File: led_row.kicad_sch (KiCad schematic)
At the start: 8 parts

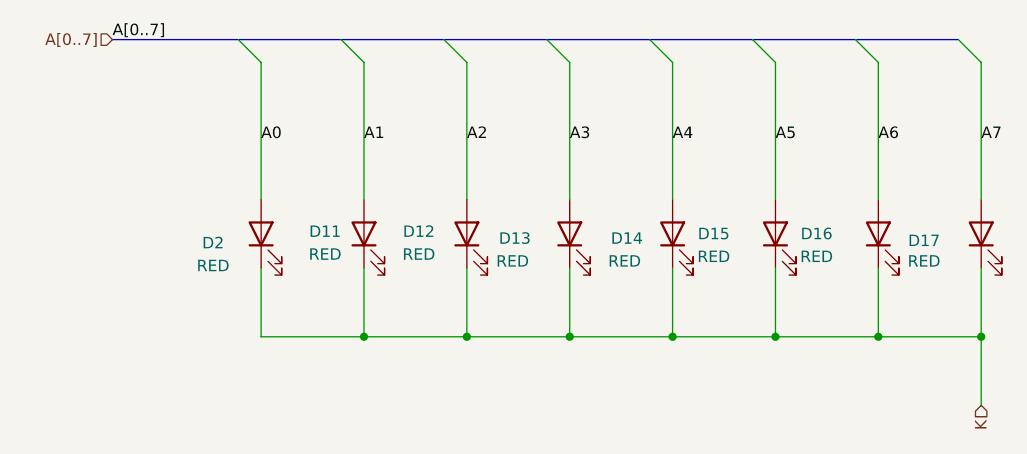
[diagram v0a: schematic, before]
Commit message: LED updates with some layout
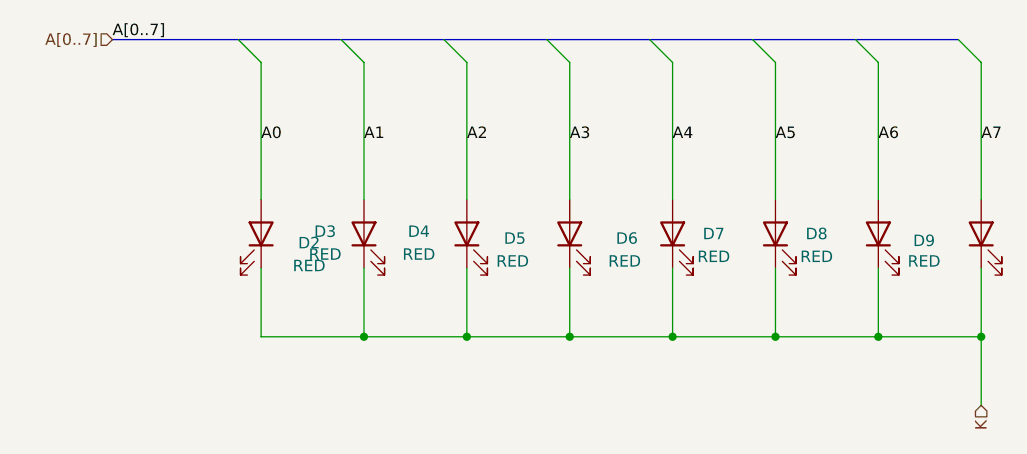
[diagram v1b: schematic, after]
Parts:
- renumbered D11 to D3, D12 to D4, D13 to D5, D14 to D6, D15 to D7, D16 to D8, D17 to D9
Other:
- moved on the sheet: D2

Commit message: LEDS wired
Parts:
- D2, D3, D4, D5, D6, D7, D8, D9: footprint LED_SMD:LED_1206_3216Metric -> LED_SMD:LED_0603_1608Metric

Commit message: Modified buck converter in schematic and pcb and got rid of old fabrication files
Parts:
- D2, D3, D4, D5, D6, D7, D8, D9: LCSC (none) -> C2286
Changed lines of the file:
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@@
 			)
 		)
+		(property "LCSC" "C2286"
+			(at 148.59 82.55 90)
+			(effects
+				(font
+					(size 1.27 1.27)
+				)
+				(hide yes)
+			)
+		)
 		(pin "1"
 		)
@@
 			)
 		)
+		(property "LCSC" "C2286"
+			(at 114.3 82.55 90)
+			(effects
+				(font
+					(size 1.27 1.27)
+				)
+				(hide yes)
+			)
+		)
 		(pin "1"
 		)
@@
 			)
 		)
+		(property "LCSC" "C2286"
+			(at 137.16 82.55 90)
+			(effects
+				(font
+					(size 1.27 1.27)
+				)
+				(hide yes)
+			)
+		)
 		(pin "1"
 		)
@@
 			)
 		)
+		(property "LCSC" "C2286"
+			(at 125.73 82.55 90)
+			(effects
+				(font
+					(size 1.27 1.27)
+				)
+				(hide yes)
+			)
+		)
 		(pin "1"
 		)
@@
 			)
 		)
+		(property "LCSC" "C2286"
+			(at 80.01 82.55 90)
+			(effects
+				(font
+					(size 1.27 1.27)
+				)
+				(hide yes)
+			)
+		)
 		(pin "1"
 		)
@@
 			)
 		)
+		(property "LCSC" "C2286"
+			(at 91.44 82.55 90)
+			(effects
+				(font
+					(size 1.27 1.27)
+				)
+				(hide yes)
+			)
+		)
 		(pin "1"
 		)
@@
 			)
 		)
+		(property "LCSC" "C2286"
+			(at 160.02 82.55 90)
+			(effects
+				(font
+					(size 1.27 1.27)
+				)
+				(hide yes)
+			)
+		)
 		(pin "1"
 		)
@@
 			(effects
 				(font
+					(size 1.27 1.27)
+				)
+				(hide yes)
+			)
+		)
+		(property "LCSC" "C2286"
+			(at 102.87 82.55 90)
+			(effects
+				(font
